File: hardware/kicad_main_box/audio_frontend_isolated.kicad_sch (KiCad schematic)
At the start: 0 parts

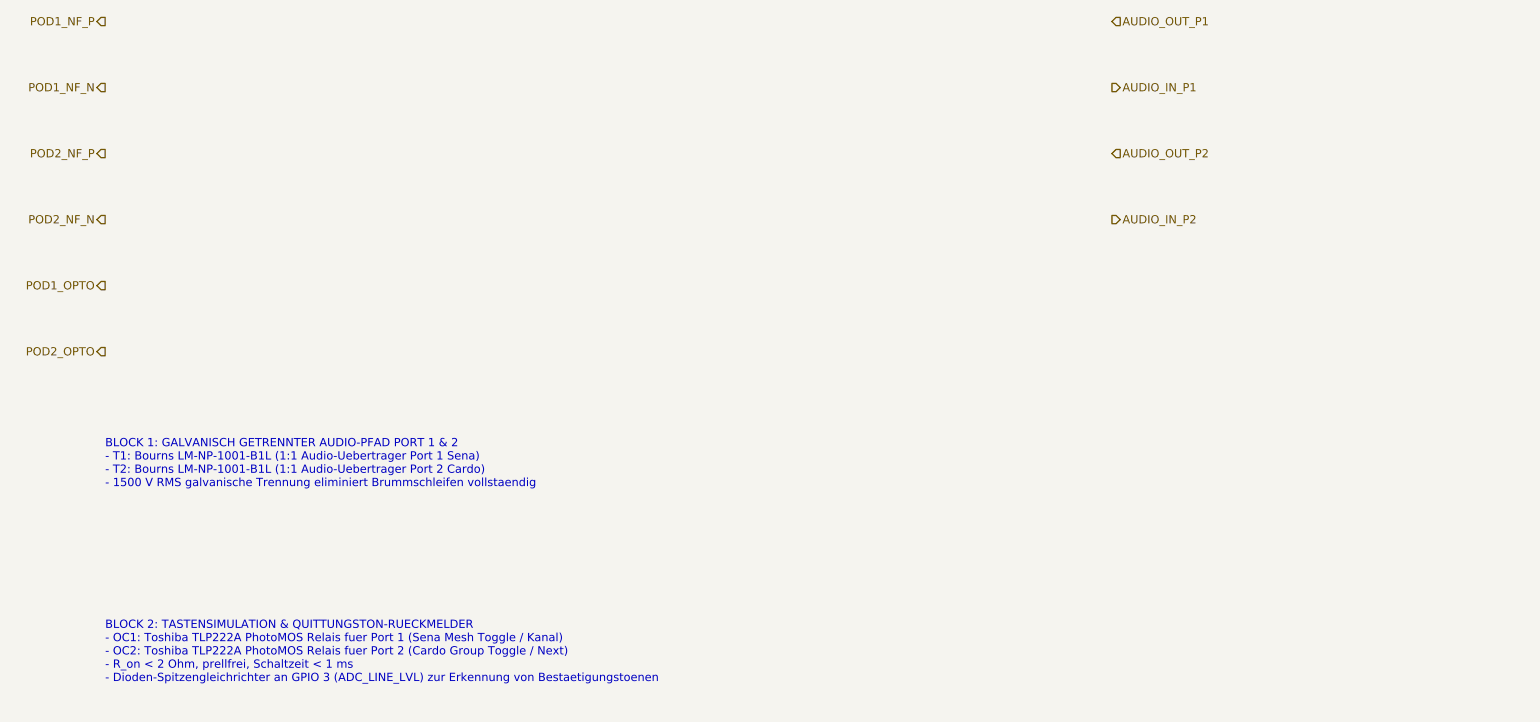
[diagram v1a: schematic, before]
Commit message: feat(kicad): Implement full graphical electronic schematic drawings (symbols, pins, wires, components) for all boards
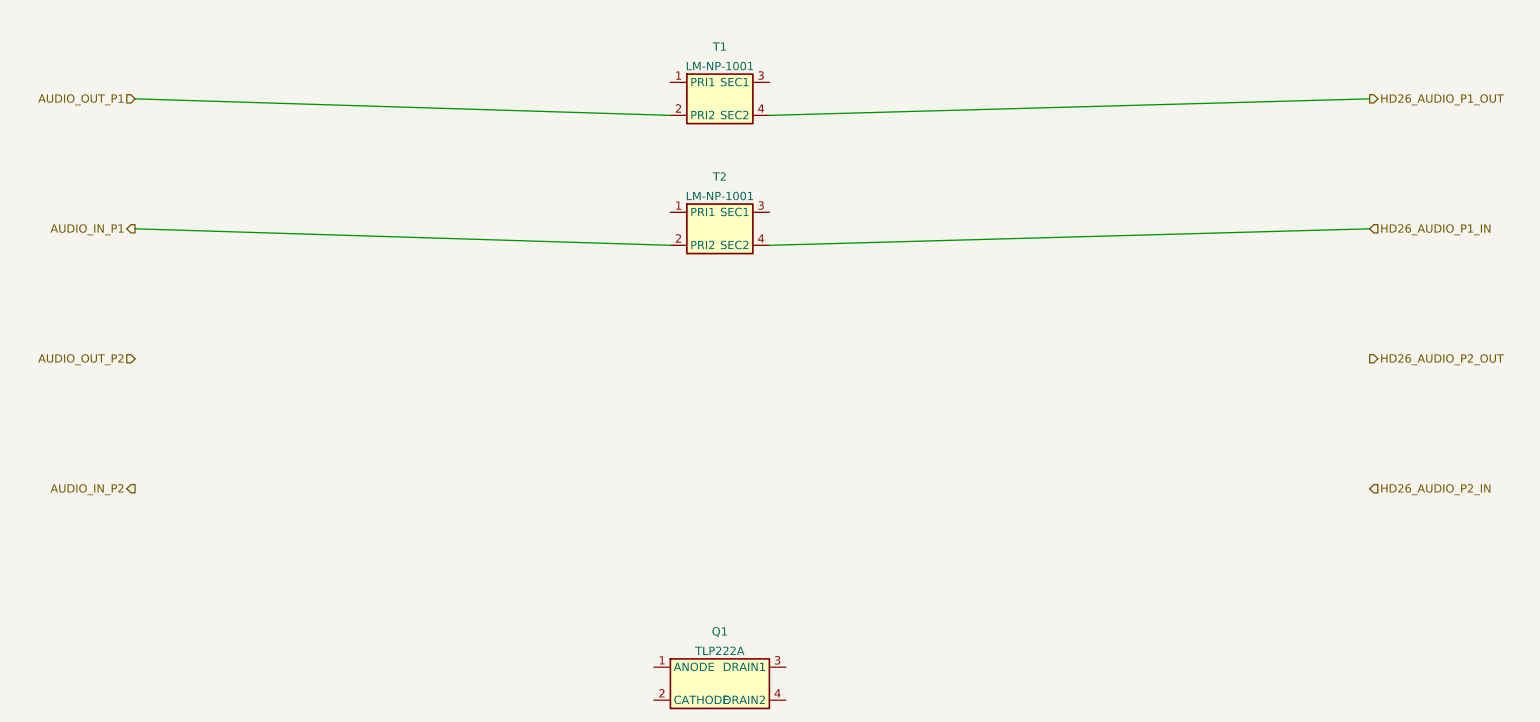
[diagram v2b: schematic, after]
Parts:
- added Q1: TLP222A, symbol Relay:TLP222A
- added T1, T2: LM-NP-1001, symbol Device:Transformer_1P_1S
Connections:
- net AUDIO_IN_P1: now also T2.2 (PRI2)
- net AUDIO_OUT_P1: now also T1.2 (PRI2)
- new net HD26_AUDIO_P1_IN: T2.4 (SEC2)
- new net HD26_AUDIO_P1_OUT: T1.4 (SEC2)
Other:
- note removed: "BLOCK 1: GALVANISCH GETRENNTER AUDIO-PFAD PORT 1 & 2 - T1: Bourns LM-NP-1001-B1L (1:1 Audio-Uebertrager Port 1 Sena) - T2: Bourns LM-NP-1001-B1L (1:1 Audio-Uebertrager Port 2 Cardo) - 1500 V RMS galvanische Trennung eliminiert Brummschleifen vollstaendig"
- note removed: "BLOCK 2: TASTENSIMULATION & QUITTUNGSTON-RUECKMELDER - OC1: Toshiba TLP222A PhotoMOS Relais fuer Port 1 (Sena Mesh Toggle / Kanal) - OC2: Toshiba TLP222A PhotoMOS Relais fuer Port 2 (Cardo Group Toggle / Next) - R_on < 2 Ohm, prellfrei, Schaltzeit < 1 ms - Dioden-Spitzengleichrichter an GPIO 3 (ADC_LINE_LVL) zur Erkennung von Bestaetigungstoenen"
- company: (none) -> OpenMotorBridge Open Source Hardware
- title: OpenMotorBridge v8.0 - Isoliertes Audio-Frontend & Optokoppler -> OpenMotorBridge v8.0 - Galvanisch Getrenntes Audio-Frontend
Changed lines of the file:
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@@
-(kicad_sch (version 20260206) (generator "eeschema") (generator_version "10.0")
-  (paper "A4")
-  (title_block
-    (title "OpenMotorBridge v8.0 - Isoliertes Audio-Frontend & Optokoppler")
-    (date "2026-08-23")
-    (rev "v8.0")
-    (comment 1 "Galvanisch getrennt ueber Bourns LM-NP-1001-B1L (1500 V RMS)")
-    (comment 2 "Prellfreie Tastensimulation via Toshiba TLP222A PhotoMOS Relais")
-  )
-  (hierarchical_label "AUDIO_OUT_P1" (shape input) (at 180.34 38.1 0)
-    (effects (font (size 1.27 1.27)) (justify left))
-  )
-  (hierarchical_label "AUDIO_IN_P1" (shape output) (at 180.34 48.26 0)
-    (effects (font (size 1.27 1.27)) (justify left))
-  )
-  (hierarchical_label "AUDIO_OUT_P2" (shape input) (at 180.34 58.42 0)
-    (effects (font (size 1.27 1.27)) (justify left))
-  )
-  (hierarchical_label "AUDIO_IN_P2" (shape output) (at 180.34 68.58 0)
-    (effects (font (size 1.27 1.27)) (justify left))
-  )
-  (hierarchical_label "POD1_NF_P" (shape output) (at 25.4 38.1 180)
-    (effects (font (size 1.27 1.27)) (justify right))
-  )
-  (hierarchical_label "POD1_NF_N" (shape output) (at 25.4 48.26 180)
-    (effects (font (size 1.27 1.27)) (justify right))
-  )
-  (hierarchical_label "POD2_NF_P" (shape output) (at 25.4 58.42 180)
-    (effects (font (size 1.27 1.27)) (justify right))
-  )
-  (hierarchical_label "POD2_NF_N" (shape output) (at 25.4 68.58 180)
-    (effects (font (size 1.27 1.27)) (justify right))
-  )
-  (hierarchical_label "POD1_OPTO" (shape output) (at 25.4 78.74 180)
-    (effects (font (size 1.27 1.27)) (justify right))
-  )
-  (hierarchical_label "POD2_OPTO" (shape output) (at 25.4 88.9 180)
-    (effects (font (size 1.27 1.27)) (justify right))
-  )
-  (text "BLOCK 1: GALVANISCH GETRENNTER AUDIO-PFAD PORT 1 & 2\n- T1: Bourns LM-NP-1001-B1L (1:1 Audio-Uebertrager Port 1 Sena)\n- T2: Bourns LM-NP-1001-B1L (1:1 Audio-Uebertrager Port 2 Cardo)\n- 1500 V RMS galvanische Trennung eliminiert Brummschleifen vollstaendig" (at 25.4 110.0 0)
-    (effects (font (size 1.27 1.27)) (justify left bottom))
-  )
-  (text "BLOCK 2: TASTENSIMULATION & QUITTUNGSTON-RUECKMELDER\n- OC1: Toshiba TLP222A PhotoMOS Relais fuer Port 1 (Sena Mesh Toggle / Kanal)\n- OC2: Toshiba TLP222A PhotoMOS Relais fuer Port 2 (Cardo Group Toggle / Next)\n- R_on < 2 Ohm, prellfrei, Schaltzeit < 1 ms\n- Dioden-Spitzengleichrichter an GPIO 3 (ADC_LINE_LVL) zur Erkennung von Bestaetigungstoenen" (at 25.4 140.0 0)
-    (effects (font (size 1.27 1.27)) (justify left bottom))
-  )
+(kicad_sch
+	(version 20260206)
+	(generator "eeschema")
+	(generator_version "10.0")
+	(paper "A3")
+	(title_block
+		(title "OpenMotorBridge v8.0 - Galvanisch Getrenntes Audio-Frontend")
+		(date "2026-08-24")
+		(rev "v8.0")
+		(company "OpenMotorBridge Open Source Hardware")
+		(comment 1 "Bourns LM-NP-1001 1:1 600 Ohm Audio-Uebertrager + Toshiba TLP222A PhotoMOS Relais")
+		(comment 2 "1.5 kV Galvanische Trennung (GND_ISO_AUDIO) zur totalen Brummschleifen-Befreiung")
+	)
+	;; =========================================================================
+	;; Hierarchical Labels
+	;; =========================================================================
+	(hierarchical_label "AUDIO_OUT_P1" (shape input) (at 30.0 50.0 180) (effects (font (size 1.27 1.27)) (justify right)))
+	(hierarchical_label "AUDIO_IN_P1" (shape output) (at 30.0 70.0 180) (effects (font (size 1.27 1.27)) (justify right)))
+	(hierarchical_label "AUDIO_OUT_P2" (shape input) (at 30.0 90.0 180) (effects (font (size 1.27 1.27)) (justify right)))
+	(hierarchical_label "AUDIO_IN_P2" (shape output) (at 30.0 110.0 180) (effects (font (size 1.27 1.27)) (justify right)))
+	(hierarchical_label "HD26_AUDIO_P1_OUT" (shape output) (at 220.0 50.0 0) (effects (font (size 1.27 1.27)) (justify left)))
+	(hierarchical_label "HD26_AUDIO_P1_IN" (shape input) (at 220.0 70.0 0) (effects (font (size 1.27 1.27)) (justify left)))
+	(hierarchical_label "HD26_AUDIO_P2_OUT" (shape output) (at 220.0 90.0 0) (effects (font (size 1.27 1.27)) (justify left)))
+	(hierarchical_label "HD26_AUDIO_P2_IN" (shape input) (at 220.0 110.0 0) (effects (font (size 1.27 1.27)) (justify left)))
+	;; =========================================================================
+	;; Symbols Placement
+	;; =========================================================================
+	;; T1: Audio Transformer Port 1 Output
+	(symbol (lib_id "Device:Transformer_1P_1S") (at 120.0 50.0 0) (unit 1)
+		(in_bom yes) (on_board yes) (dnp no)
+		(property "Reference" "T1" (at 120.0 42.0 0) (effects (font (size 1.27 1.27))))
+		(property "Value" "LM-NP-1001" (at 120.0 45.0 0) (effects (font (size 1.27 1.27))))
+		(pin "1")
+		(pin "2")
+		(pin "3")
+		(pin "4")
+	)
+	;; T2: Audio Transformer Port 1 Input
+	(symbol (lib_id "Device:Transformer_1P_1S") (at 120.0 70.0 0) (unit 1)
+		(in_bom yes) (on_board yes) (dnp no)
+		(property "Reference" "T2" (at 120.0 62.0 0) (effects (font (size 1.27 1.27))))
+		(property "Value" "LM-NP-1001" (at 120.0 65.0 0) (effects (font (size 1.27 1.27))))
+		(pin "1")
+		(pin "2")
+		(pin "3")
+		(pin "4")
+	)
+	;; Q1: TLP222A PhotoMOS Opto Relay Port 1
+	(symbol (lib_id "Relay:TLP222A") (at 120.0 140.0 0) (unit 1)
+		(in_bom yes) (on_board yes) (dnp no)
+		(property "Reference" "Q1" (at 120.0 132.0 0) (effects (font (size 1.27 1.27))))
+		(property "Value" "TLP222A" (at 120.0 135.0 0) (effects (font (size 1.27 1.27))))
+		(pin "1")
+		(pin "2")
+		(pin "3")
+		(pin "4")
+	)
+	;; =========================================================================
+	;; Interconnecting Wires
+	;; =========================================================================
+	(wire (pts (xy 30.0 50.0) (xy 112.38 52.54)) (stroke (width 0) (type solid)))
+	(wire (pts (xy 127.62 52.54) (xy 220.0 50.0)) (stroke (width 0) (type solid)))
+	(wire (pts (xy 30.0 70.0) (xy 112.38 72.54)) (stroke (width 0) (type solid)))
+	(wire (pts (xy 127.62 72.54) (xy 220.0 70.0)) (stroke (width 0) (type solid)))
 )

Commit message: fix(kicad): Synchronize hierarchical sheet pins with child hierarchical labels across all sub-schematics
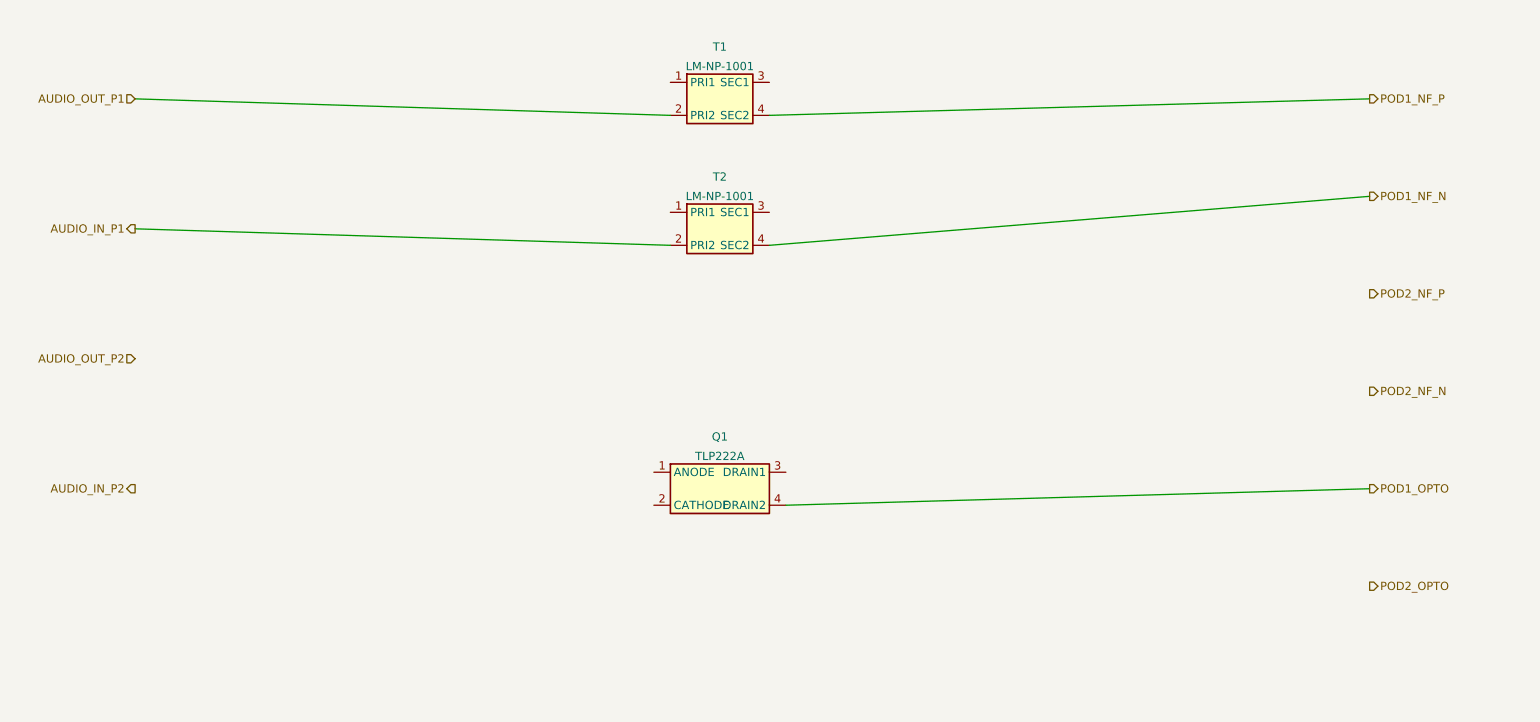
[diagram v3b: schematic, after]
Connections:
- net POD1_OPTO: now reaches Q1.4 (DRAIN2)
- net HD26_AUDIO_P1_IN renamed POD1_NF_N
- net HD26_AUDIO_P1_OUT renamed POD1_NF_P
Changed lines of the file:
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@@
 	)
 	;; =========================================================================
-	;; Hierarchical Labels
+	;; Hierarchical Labels (Matching Parent Sheet Pins exactly)
 	;; =========================================================================
 	(hierarchical_label "AUDIO_OUT_P1" (shape input) (at 30.0 50.0 180) (effects (font (size 1.27 1.27)) (justify right)))
@@
 	(hierarchical_label "AUDIO_OUT_P2" (shape input) (at 30.0 90.0 180) (effects (font (size 1.27 1.27)) (justify right)))
 	(hierarchical_label "AUDIO_IN_P2" (shape output) (at 30.0 110.0 180) (effects (font (size 1.27 1.27)) (justify right)))
-	(hierarchical_label "HD26_AUDIO_P1_OUT" (shape output) (at 220.0 50.0 0) (effects (font (size 1.27 1.27)) (justify left)))
-	(hierarchical_label "HD26_AUDIO_P1_IN" (shape input) (at 220.0 70.0 0) (effects (font (size 1.27 1.27)) (justify left)))
-	(hierarchical_label "HD26_AUDIO_P2_OUT" (shape output) (at 220.0 90.0 0) (effects (font (size 1.27 1.27)) (justify left)))
-	(hierarchical_label "HD26_AUDIO_P2_IN" (shape input) (at 220.0 110.0 0) (effects (font (size 1.27 1.27)) (justify left)))
+	(hierarchical_label "POD1_NF_P" (shape output) (at 220.0 50.0 0) (effects (font (size 1.27 1.27)) (justify left)))
+	(hierarchical_label "POD1_NF_N" (shape output) (at 220.0 65.0 0) (effects (font (size 1.27 1.27)) (justify left)))
+	(hierarchical_label "POD2_NF_P" (shape output) (at 220.0 80.0 0) (effects (font (size 1.27 1.27)) (justify left)))
+	(hierarchical_label "POD2_NF_N" (shape output) (at 220.0 95.0 0) (effects (font (size 1.27 1.27)) (justify left)))
+	(hierarchical_label "POD1_OPTO" (shape output) (at 220.0 110.0 0) (effects (font (size 1.27 1.27)) (justify left)))
+	(hierarchical_label "POD2_OPTO" (shape output) (at 220.0 125.0 0) (effects (font (size 1.27 1.27)) (justify left)))
 	;; =========================================================================
 	;; Symbols Placement
@@
 	)
 	;; Q1: TLP222A PhotoMOS Opto Relay Port 1
-	(symbol (lib_id "Relay:TLP222A") (at 120.0 140.0 0) (unit 1)
+	(symbol (lib_id "Relay:TLP222A") (at 120.0 110.0 0) (unit 1)
 		(in_bom yes) (on_board yes) (dnp no)
-		(property "Reference" "Q1" (at 120.0 132.0 0) (effects (font (size 1.27 1.27))))
-		(property "Value" "TLP222A" (at 120.0 135.0 0) (effects (font (size 1.27 1.27))))
+		(property "Reference" "Q1" (at 120.0 102.0 0) (effects (font (size 1.27 1.27))))
+		(property "Value" "TLP222A" (at 120.0 105.0 0) (effects (font (size 1.27 1.27))))
 		(pin "1")
 		(pin "2")
@@
 	(wire (pts (xy 127.62 52.54) (xy 220.0 50.0)) (stroke (width 0) (type solid)))
 	(wire (pts (xy 30.0 70.0) (xy 112.38 72.54)) (stroke (width 0) (type solid)))
-	(wire (pts (xy 127.62 72.54) (xy 220.0 70.0)) (stroke (width 0) (type solid)))
+	(wire (pts (xy 127.62 72.54) (xy 220.0 65.0)) (stroke (width 0) (type solid)))
+	(wire (pts (xy 130.16 112.54) (xy 220.0 110.0)) (stroke (width 0) (type solid)))
 )
